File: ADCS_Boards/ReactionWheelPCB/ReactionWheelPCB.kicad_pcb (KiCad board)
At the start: 4 copper layers, 90.2 x 95.9 mm, 13 parts, among them J1 PC104_Connector, U1 Conn_1, U2 Conn_1, U3 Controller 1, U4 Controller 2, U5 Controller 3, U6 Controller 4, U7 Conn_1, U8 Conn_1

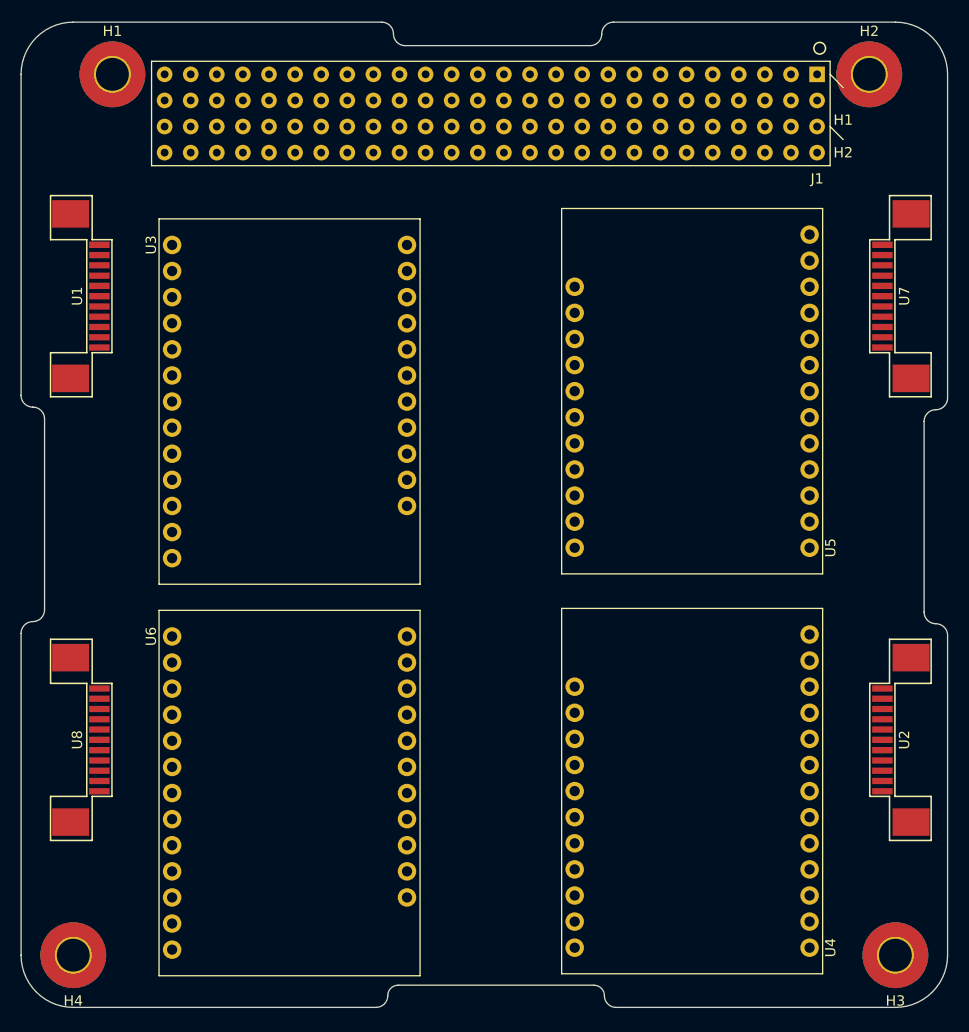
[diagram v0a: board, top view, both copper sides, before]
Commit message: Updated RW and MCU PCBS. Layouts are complete, just need to do routing. (Pushed for Yasin Shahrami)
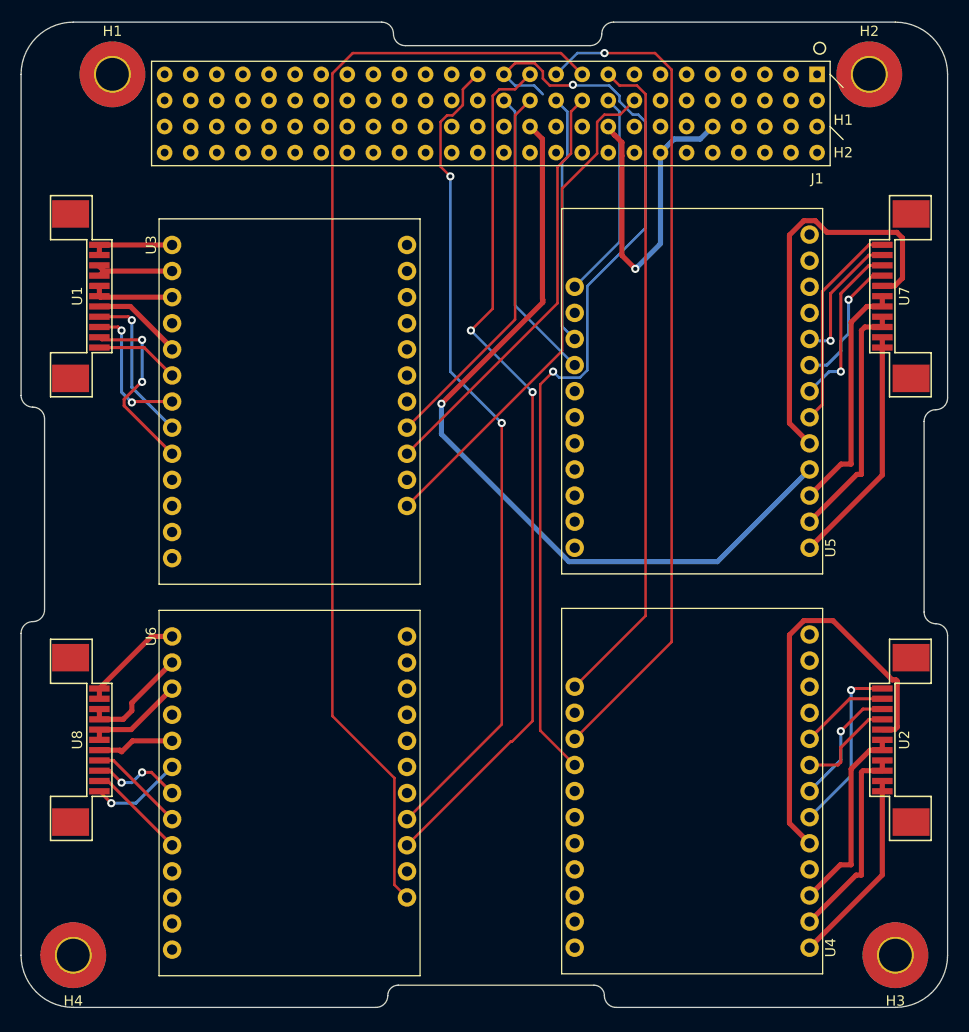
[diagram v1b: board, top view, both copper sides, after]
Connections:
- net 3V3 renamed +3.3V
- net 5V renamed +5V
- net Net-(J1-Pad75) renamed +12V
- J1 pad 28: ACA(S1) -> unconnected-(J1-Pad28)
- J1 pad 29: ACA(S2) -> unconnected-(J1-Pad29)
- J1 pad 30: ACA(S3) -> unconnected-(J1-Pad30)
- J1 pad 31: ACA(S4) -> unconnected-(J1-Pad31)
- J1 pad 33: ASA(S1) -> unconnected-(J1-Pad33)
- J1 pad 34: ASA(S2) -> unconnected-(J1-Pad34)
- J1 pad 35: ASA(S3) -> unconnected-(J1-Pad35)
- J1 pad 36: ASA(S4) -> unconnected-(J1-Pad36)
- U3 pad 19: ACA(S1) -> unconnected-(U3-Pad19)
- U3 pad 20: ASA(S1) -> unconnected-(U3-Pad20)
- U4 pad 19: ACA(S2) -> unconnected-(U4-Pad19)
- U4 pad 20: ASA(S2) -> unconnected-(U4-Pad20)
- U5 pad 19: ACA(S3) -> unconnected-(U5-Pad19)
- U5 pad 20: ASA(S3) -> unconnected-(U5-Pad20)
- U6 pad 19: ACA(S4) -> unconnected-(U6-Pad19)
- U6 pad 20: ACA(S4) -> unconnected-(U6-Pad20)
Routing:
- net GND: track 0.00 -> 130.0 mm, vias 0 -> 1
- net Enable(S4): track 0.00 -> 109.2 mm
- net PWM-SetValue(S2): track 0.00 -> 92.6 mm, vias 0 -> 2
- net Direction(S4): track 0.00 -> 85.9 mm, vias 0 -> 2
- net Direction(S2): track 0.00 -> 81.8 mm, vias 0 -> 1
- net PWM-SetValue(S4): track 0.00 -> 80.6 mm, vias 0 -> 2
- net +12V: track 0.00 -> 79.2 mm, vias 0 -> 1
- net Enable(S2): track 0.00 -> 65.0 mm
- net Enable(S1): track 0.00 -> 49.5 mm
- net Direction(S1): track 0.00 -> 41.4 mm
- net PWM-SetValue(S1): track 0.00 -> 36.8 mm
- net PWM-SetValue(S3): track 0.00 -> 28.6 mm
- net Direction(S3): track 0.00 -> 24.4 mm
- net Net-(U5-Pad2): track 0.00 -> 24.1 mm
- net Net-(U5-Pad3): track 0.00 -> 23.8 mm
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- added copper zone on In2.Cu, net +12V
- added copper zone on In1.Cu, net GND
